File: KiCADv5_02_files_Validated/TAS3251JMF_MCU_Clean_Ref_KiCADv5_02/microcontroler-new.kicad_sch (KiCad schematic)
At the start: 8 parts, among them J14 USB_C_Receptacle_USB2.0_14P, U4 ESP32-S3-WROOM-1, U6 USBLC6-2SC6

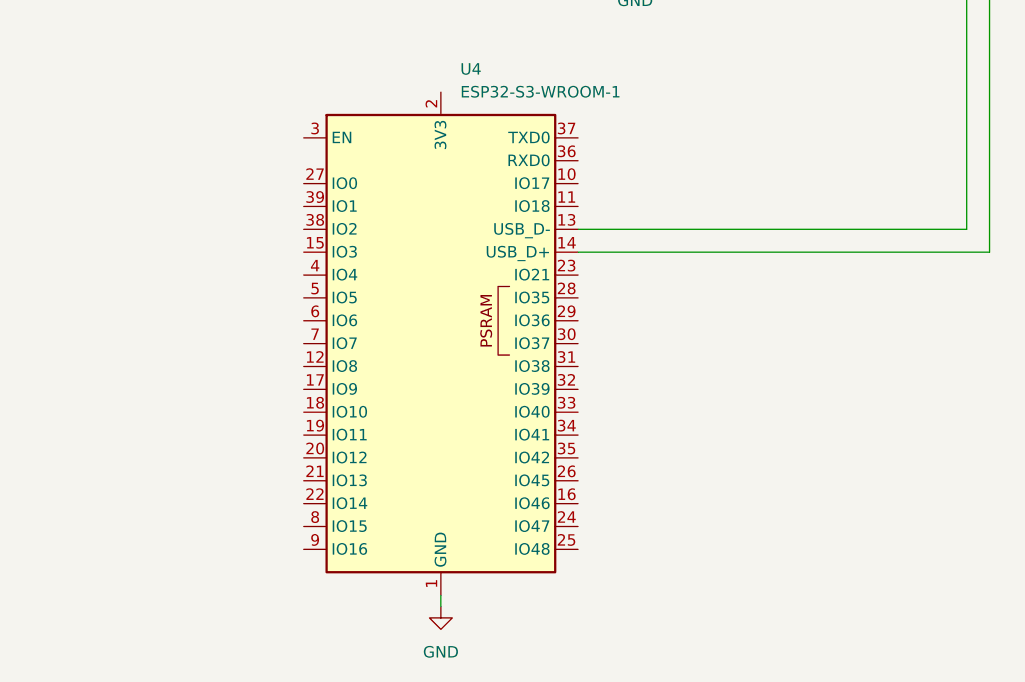
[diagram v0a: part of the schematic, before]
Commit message: Adding signals to control for new uC
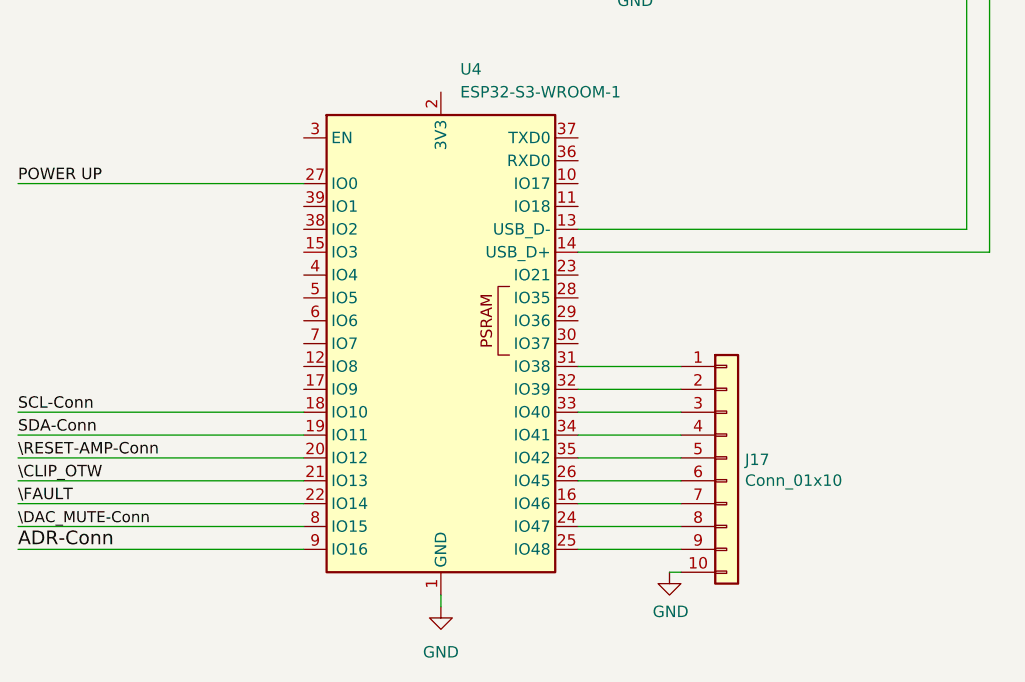
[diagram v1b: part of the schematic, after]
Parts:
- added J17: Conn_01x10, Connector_PinHeader_2.54mm:PinHeader_1x10_P2.54mm_Vertical, symbol Connector_Generic:Conn_01x10
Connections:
- net GND: now also J17.10 (Pin_10)
- net at U4.16 (IO46): now also J17.7 (Pin_7)
- net SCL-Conn: now reaches U4.18 (IO10)
- net SDA-Conn: now reaches U4.19 (IO11)
- net \RESET-AMP-Conn: now reaches U4.20 (IO12)
- net \CLIP_OTW: now reaches U4.21 (IO13)
- net \FAULT: now reaches U4.22 (IO14)
- net at U4.24 (IO47): now also J17.8 (Pin_8)
- net at U4.25 (IO48): now also J17.9 (Pin_9)
- net at U4.26 (IO45): now also J17.6 (Pin_6)
- net POWER UP: now reaches U4.27 (IO0)
- net at U4.31 (IO38): now also J17.1 (Pin_1)
- net at U4.32 (IO39): now also J17.2 (Pin_2)
- net at U4.33 (IO40): now also J17.3 (Pin_3)
- net at U4.34 (IO41): now also J17.4 (Pin_4)
- net at U4.35 (IO42): now also J17.5 (Pin_5)
- net \DAC_MUTE-Conn: now reaches U4.8 (IO15)
- net ADR-Conn: now reaches U4.9 (IO16)

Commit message: modified PSU
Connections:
- net 15V_PGOOD: now reaches U4.30 (IO37)
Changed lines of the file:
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@@
+	(wire
+		(pts
+			(xy 116.84 106.68) (xy 139.7 106.68)
+		)
+		(stroke
+			(width 0)
+			(type default)
+		)
+	)
 	(wire
 		(pts
@@
 			(effects
 				(font
+					(size 1.27 1.27)
+				)
+				(justify left)
+				(hide yes)
+			)
+		)
+	)
+	(global_label "15V_PGOOD"
+		(shape input)
+		(at 139.7 106.68 0)
+		(fields_autoplaced yes)
+		(effects
+			(font
+				(size 1.27 1.27)
+			)
+			(justify left)
+		)
+		(property "Intersheetrefs" "${INTERSHEET_REFS}"
+			(at 152.9772 106.68 0)
+			(effects
+				(font
